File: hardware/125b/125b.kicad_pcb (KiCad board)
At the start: 2 copper layers, 54 x 60 mm, 56 parts, among them J1 Guitar in, J2 fsw pin 1, J3 fsw pin 2, J4 fsw pin 4, J5 fsw pin 5, J6 fsw pin 6, J7 Left out, J8 Right out, J9 fsw pin 3, SW1 Switch 1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

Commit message: Update PCB and resize for 125b
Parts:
- added J10: Barrel_Jack, Connector_BarrelJack:BarrelJack_Horizontal, F.Cu at (58.1, 52.3)
- added J11: NRJ6HF, Connector_Audio:Jack_6.35mm_Neutrik_NRJ6HF_Horizontal, F.Cu at (51.9, 32.2)
- added J7: fsw pin 3, Connector_Wire:SolderWire-0.25sqmm_1x01_D0.65mm_OD2mm, F.Cu at (75.5, 49.0)
- added J8: fsw pin 4, Connector_Wire:SolderWire-0.25sqmm_1x01_D0.65mm_OD2mm, F.Cu at (75.5, 53.0)
- added SW4: SW_DIP_x02, Button_Switch_SMD:SW_DIP_SPSTx02_Slide_9.78x7.26mm_W8.61mm_P2.54mm, F.Cu at (66.9, 51.4)
- J2: value fsw pin 1 -> fsw pin 7
- J4: value fsw pin 4 -> fsw pin 7
- J9: value fsw pin 3 -> fsw pin 1
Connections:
- C2 pad 1: Net-(J4-Pin_1) -> Net-(C2-Pad1)
- D2 pad 2: Net-(BT1-+) -> Net-(D2-A)
- R1 pad 1: Net-(BT1-+) -> Net-(D2-A)
- R2 pad 1: Net-(J4-Pin_1) -> Net-(C2-Pad1)
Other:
- board size 54 x 60 mm -> 59 x 75 mm

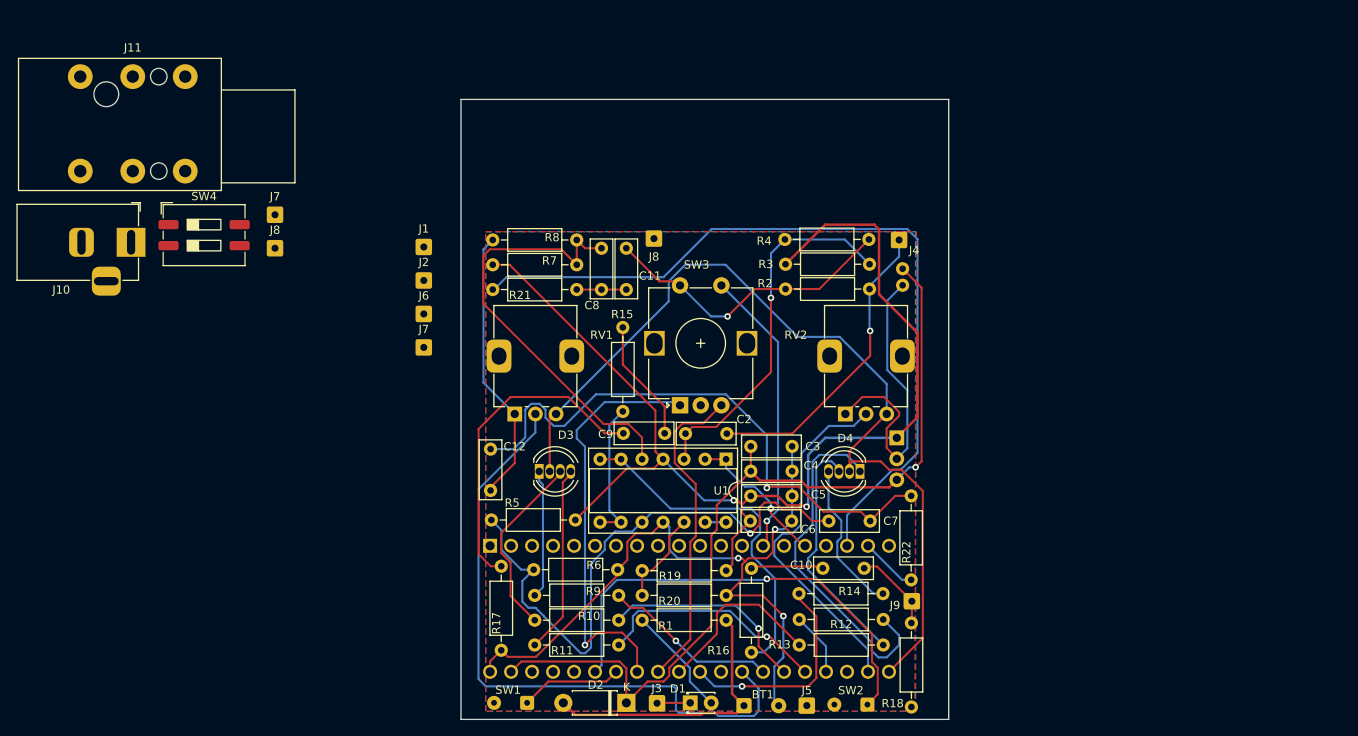
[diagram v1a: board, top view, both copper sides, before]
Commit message: Footprints for audio and power sockets added
Also DIP switch for line/ guitar input. Ready to start
moving components around.
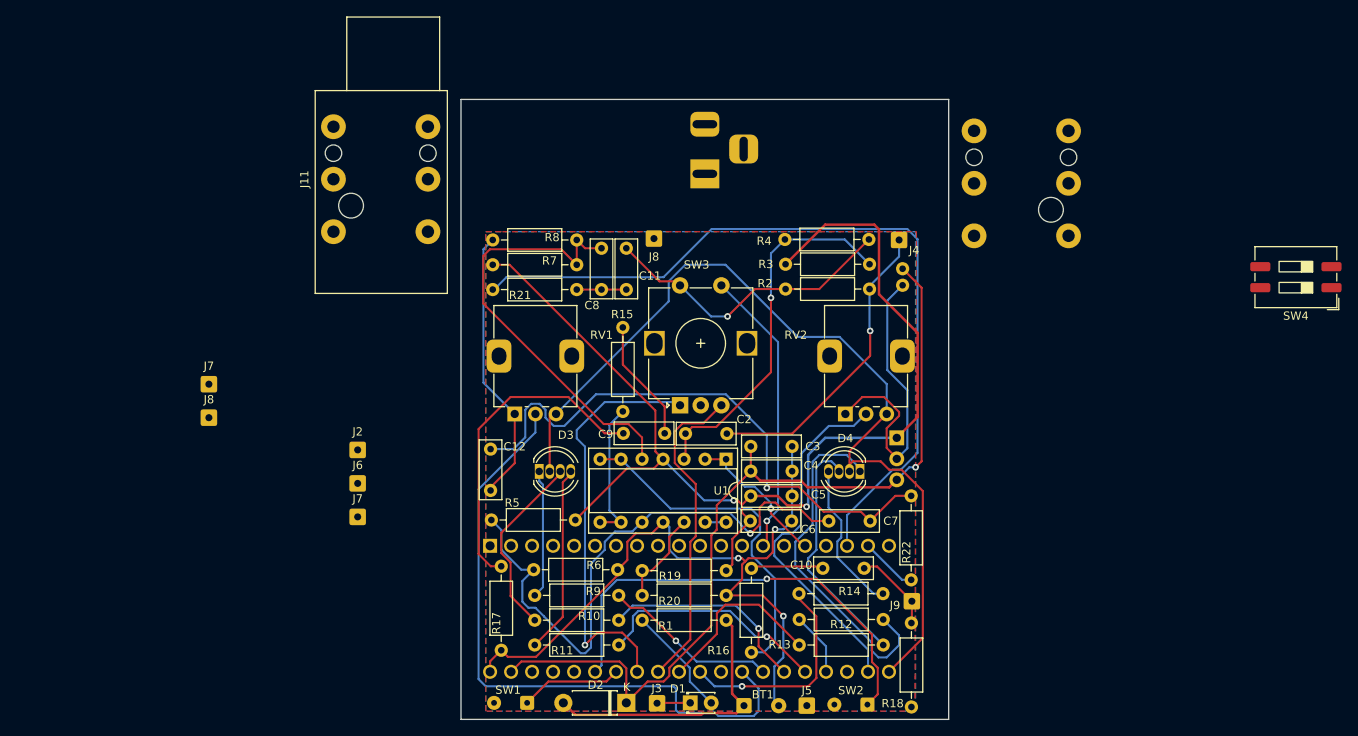
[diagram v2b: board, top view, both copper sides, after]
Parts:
- J1: footprint Connector_Wire:SolderWire-0.25sqmm_1x01_D0.65mm_OD2mm -> Connector_Audio:Jack_6.35mm_Neutrik_NRJ6HF-1-AU_Horizontal; moved to B.Cu
- J10: moved to B.Cu
- moved SW4 132.2 mm to (199.0, 56.5), turned to 180 degrees
- moved J1 78.0 mm to (171.5, 51.5), turned to 90 degrees
- moved J10 69.9 mm to (127.5, 44.0), turned to -90 degrees
- moved J11 35.9 mm to (82.6, 51.0), turned to 90 degrees
- moved J2 22.0 mm to (85.5, 77.4)
- moved J6 22.0 mm to (85.5, 81.5)
- moved J7 22.0 mm to (67.5, 69.5)
- moved J7 22.0 mm to (85.5, 85.5)
- moved J8 22.0 mm to (67.5, 73.5)

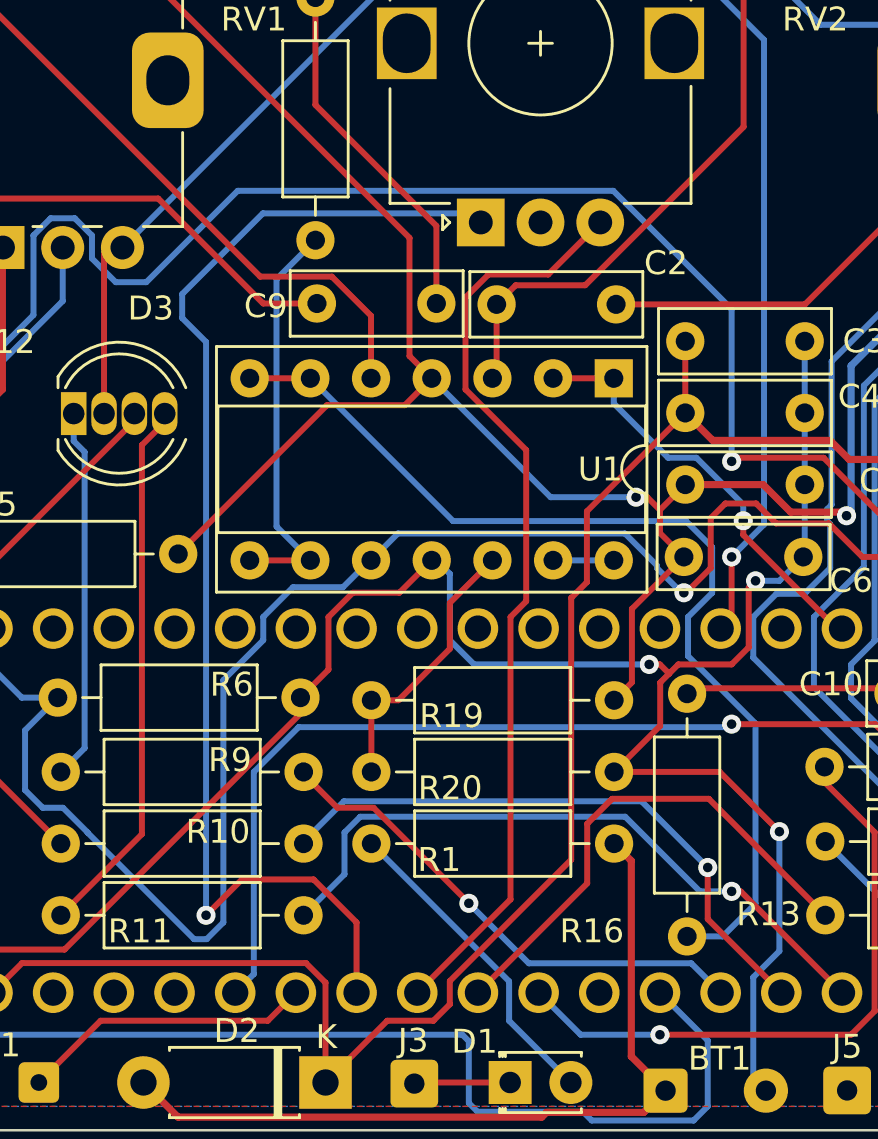
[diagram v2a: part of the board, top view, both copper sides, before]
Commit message: Swap encoder pins
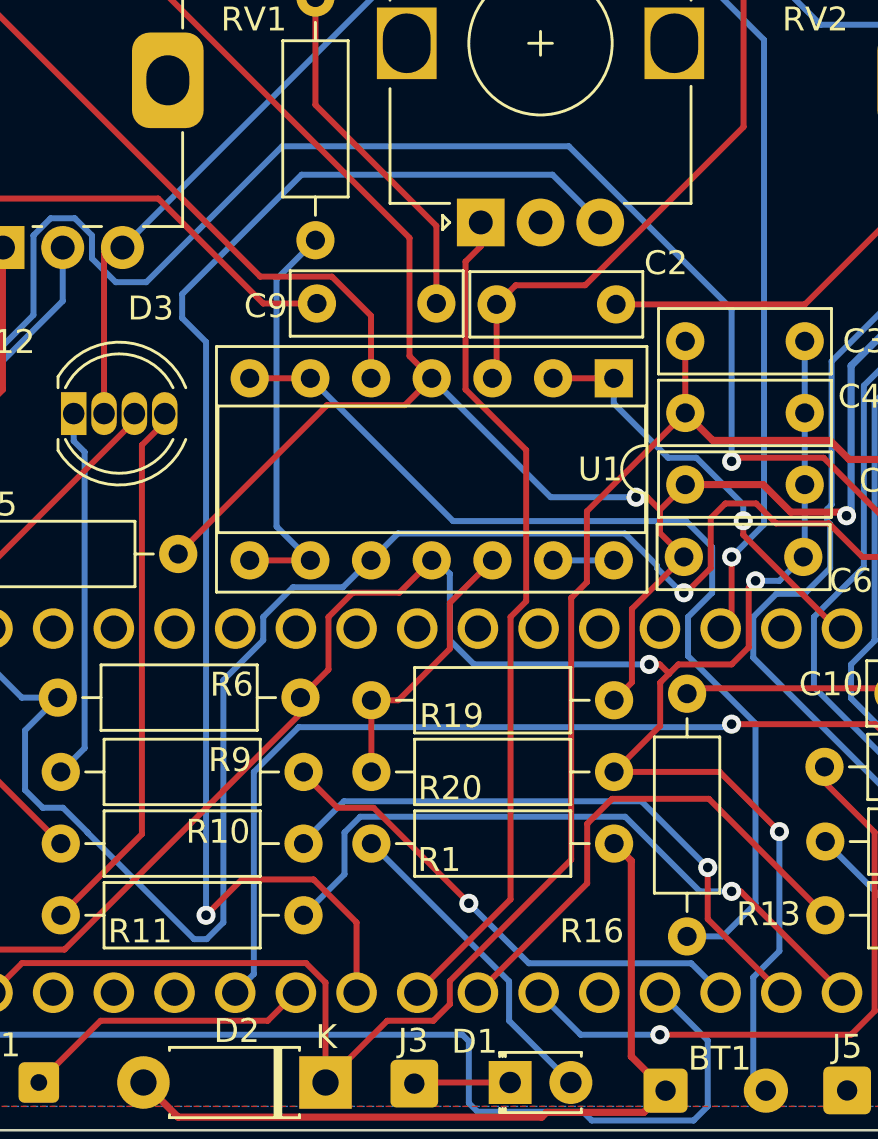
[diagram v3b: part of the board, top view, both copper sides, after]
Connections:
- A1 pad 32: Net-(A1-SAI2_SD_B) -> /ENC_A
- A1 pad 33: Net-(A1-SAI2_SD_A) -> /ENC_B
- SW3 pad A: Net-(A1-SAI2_SD_A) -> /ENC_A
- SW3 pad B: Net-(A1-SAI2_SD_B) -> /ENC_B
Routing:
- net /ENC_B: track 0.00 -> 57.4 mm, vias 0 -> 1
- net Net-(A1-SAI2_SD_A): track 52.0 -> 0.00 mm, vias 1 -> 0
- net Net-(A1-SAI2_SD_B): track 39.0 -> 0.00 mm
- net /ENC_A: track 0.00 -> 36.3 mm
- net Net-(C12-Pad2): track 69.8 -> 71.4 mm
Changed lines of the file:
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@@
 	(net 30 "/LED_2_B")
 	(net 31 "/LED_2_G")
-	(net 32 "Net-(A1-SAI2_SD_B)")
-	(net 33 "Net-(A1-SAI2_SD_A)")
+	(net 32 "/ENC_B")
+	(net 33 "/ENC_A")
 	(net 34 "Net-(A1-SAI2_FS)")
 	(net 35 "Net-(A1-SAI2_SCK)")
@@
 			(layers "*.Cu" "*.Mask")
 			(remove_unused_layers no)
-			(net 33 "Net-(A1-SAI2_SD_A)")
+			(net 33 "/ENC_A")
 			(pinfunction "A")
 			(pintype "passive")
@@
 			(layers "*.Cu" "*.Mask")
 			(remove_unused_layers no)
-			(net 32 "Net-(A1-SAI2_SD_B)")
+			(net 32 "/ENC_B")
 			(pinfunction "B")
 			(pintype "passive")
@@
 			(layers "*.Cu" "*.Mask")
 			(remove_unused_layers no)
-			(net 32 "Net-(A1-SAI2_SD_B)")
+			(net 33 "/ENC_A")
 			(pinfunction "SAI2_SD_B")
 			(pintype "bidirectional")
@@
 			(layers "*.Cu" "*.Mask")
 			(remove_unused_layers no)
-			(net 33 "Net-(A1-SAI2_SD_A)")
+			(net 32 "/ENC_B")
 			(pinfunction "SAI2_SD_A")
 			(pintype "bidirectional")
@@
 	)
 	(segment
-		(start 123.861294 78.98953)
-		(end 126.401294 81.52953)
+		(start 114.5 99.5)
+		(end 117.5 99.5)
 		(width 0.25)
 		(layer "F.Cu")
@@
 	)
 	(segment
-		(start 125.745 88.513299)
-		(end 125.745 100.335)
+		(start 113 101)
+		(end 114.5 99.5)
 		(width 0.25)
 		(layer "F.Cu")
@@
 	)
 	(segment
-		(start 123.861294 75.138992)
-		(end 123.861294 78.98953)
+		(start 119.3 101.3)
+		(end 119.3 104.24)
 		(width 0.25)
 		(layer "F.Cu")
@@
 	)
 	(segment
-		(start 126.401294 81.52953)
-		(end 126.401294 87.857005)
+		(start 117.5 99.5)
+		(end 119.3 101.3)
 		(width 0.25)
 		(layer "F.Cu")
 		(net 32)
 	)
-	(segment
-		(start 124.821859 74.178427)
-		(end 123.861294 75.138992)
-		(width 0.25)
-		(layer "F.Cu")
+	(via
+		(at 113 101)
+		(size 0.8)
+		(drill 0.4)
+		(layers "F.Cu" "B.Cu")
 		(net 32)
 	)
 	(segment
-		(start 127.321573 74.178427)
-		(end 124.821859 74.178427)
+		(start 112 75)
+		(end 117 70)
 		(width 0.25)
-		(layer "F.Cu")
+		(layer "B.Cu")
 		(net 32)
 	)
 	(segment
-		(start 125.745 100.335)
-		(end 121.84 104.24)
+		(start 112 76)
+		(end 112 75)
 		(width 0.25)
-		(layer "F.Cu")
+		(layer "B.Cu")
 		(net 32)
 	)
 	(segment
-		(start 129.5 72)
-		(end 127.321573 74.178427)
+		(start 117 70)
+		(end 127.5 70)
 		(width 0.25)
-		(layer "F.Cu")
+		(layer "B.Cu")
 		(net 32)
 	)
 	(segment
-		(start 126.401294 87.857005)
-		(end 125.745 88.513299)
+		(start 113 101)
+		(end 113 77)
 		(width 0.25)
-		(layer "F.Cu")
+		(layer "B.Cu")
 		(net 32)
 	)
 	(segment
-		(start 114.5 99.5)
-		(end 117.5 99.5)
+		(start 127.5 70)
+		(end 129.5 72)
 		(width 0.25)
-		(layer "F.Cu")
-		(net 33)
+		(layer "B.Cu")
+		(net 32)
 	)
 	(segment
-		(start 113 101)
-		(end 114.5 99.5)
+		(start 113 77)
+		(end 112 76)
 		(width 0.25)
-		(layer "F.Cu")
-		(net 33)
+		(layer "B.Cu")
+		(net 32)
 	)
 	(segment
-		(start 119.3 101.3)
-		(end 119.3 104.24)
+		(start 126.401294 81.52953)
+		(end 123.861294 78.98953)
 		(width 0.25)
 		(layer "F.Cu")
@@
 	)
 	(segment
-		(start 117.5 99.5)
-		(end 119.3 101.3)
+		(start 126.401294 87.857005)
+		(end 126.401294 81.52953)
 		(width 0.25)
 		(layer "F.Cu")
 		(net 33)
 	)
-	(via
-		(at 113 101)
-		(size 0.8)
-		(drill 0.4)
-		(layers "F.Cu" "B.Cu")
-		(net 33)
-	)
 	(segment
-		(start 112 75)
-		(end 112 76)
+		(start 124.5 73)
+		(end 124.5 72)
 		(width 0.25)
-		(layer "B.Cu")
+		(layer "F.Cu")
 		(net 33)
 	)
 	(segment
-		(start 115.381396 71.618604)
-		(end 112 75)
+		(start 123.861294 73.638706)
+		(end 124.5 73)
 		(width 0.25)
-		(layer "B.Cu")
+		(layer "F.Cu")
 		(net 33)
 	)
 	(segment
-		(start 124.118604 71.618604)
-		(end 115.381396 71.618604)
+		(start 123.861294 78.98953)
+		(end 123.861294 73.638706)
 		(width 0.25)
-		(layer "B.Cu")
+		(layer "F.Cu")
 		(net 33)
 	)
 	(segment
-		(start 124.5 72)
-		(end 124.118604 71.618604)
+		(start 125.745 100.335)
+		(end 125.745 88.513299)
 		(width 0.25)
-		(layer "B.Cu")
+		(layer "F.Cu")
 		(net 33)
 	)
 	(segment
-		(start 113 77)
-		(end 113 101)
+		(start 121.84 104.24)
+		(end 125.745 100.335)
 		(width 0.25)
-		(layer "B.Cu")
+		(layer "F.Cu")
 		(net 33)
 	)
 	(segment
-		(start 124.5 72)
-		(end 123.861294 72.638706)
+		(start 125.745 88.513299)
+		(end 126.401294 87.857005)
 		(width 0.25)
-		(layer "B.Cu")
+		(layer "F.Cu")
 		(net 33)
 	)
 	(segment
-		(start 112 76)
-		(end 113 77)
+		(start 123.861294 72.638706)
+		(end 124.5 72)
 		(width 0.25)
 		(layer "B.Cu")
@@
 	)
 	(segment
-		(start 101.576468 77.302941)
-		(end 104.349081 77.302941)
+		(start 107.507412 71.825)
+		(end 108.225 72.542588)
 		(width 0.25)
 		(layer "B.Cu")
@@
 	)
 	(segment
-		(start 135 75.626167)
-		(end 135 82)
+		(start 128.186966 68.813133)
+		(end 135 75.626167)
 		(width 0.25)
 		(layer "B.Cu")
@@
 	)
 	(segment
-		(start 109.217588 74.5)
-		(end 110.5 74.5)
+		(start 135 75.626167)
+		(end 135 82)
 		(width 0.25)
 		(layer "B.Cu")
@@
 	)
 	(segment
-		(start 110.5 74.5)
-		(end 114.325 70.675)
+		(start 101.576468 77.302941)
+		(end 104.349081 77.302941)
 		(width 0.25)
 		(layer "B.Cu")
@@
 	)
 	(segment
-		(start 108.225 72.542588)
-		(end 108.225 73.507412)
+		(start 104.349081 77.302941)
+		(end 105.775 75.877022)
 		(width 0.25)
 		(layer "B.Cu")
@@
 	)
 	(segment
-		(start 130.048833 70.675)
-		(end 135 75.626167)
+		(start 109.217588 74.5)
+		(end 110.5 74.5)
 		(width 0.25)
 		(layer "B.Cu")
@@
 	)
 	(segment
-		(start 105.775 72.542588)
-		(end 106.492588 71.825)
+		(start 116.186867 68.813133)
+		(end 128.186966 68.813133)
 		(width 0.25)
 		(layer "B.Cu")
@@
 	)
 	(segment
-		(start 104.349081 77.302941)
-		(end 105.775 75.877022)
+		(start 110.5 74.5)
+		(end 116.186867 68.813133)
 		(width 0.25)
 		(layer "B.Cu")
@@
 	)
 	(segment
-		(start 114.325 70.675)
-		(end 130.048833 70.675)
+		(start 105.775 72.542588)
+		(end 106.492588 71.825)
 		(width 0.25)
 		(layer "B.Cu")
@@
 	)
 	(segment
-		(start 108.225 73.507412)
-		(end 109.217588 74.5)
+		(start 108.225 72.542588)
+		(end 108.225 73.507412)
 		(width 0.25)
 		(layer "B.Cu")
@@
 	)
 	(segment
-		(start 107.507412 71.825)
-		(end 108.225 72.542588)
+		(start 108.225 73.507412)
+		(end 109.217588 74.5)
 		(width 0.25)
 		(layer "B.Cu")

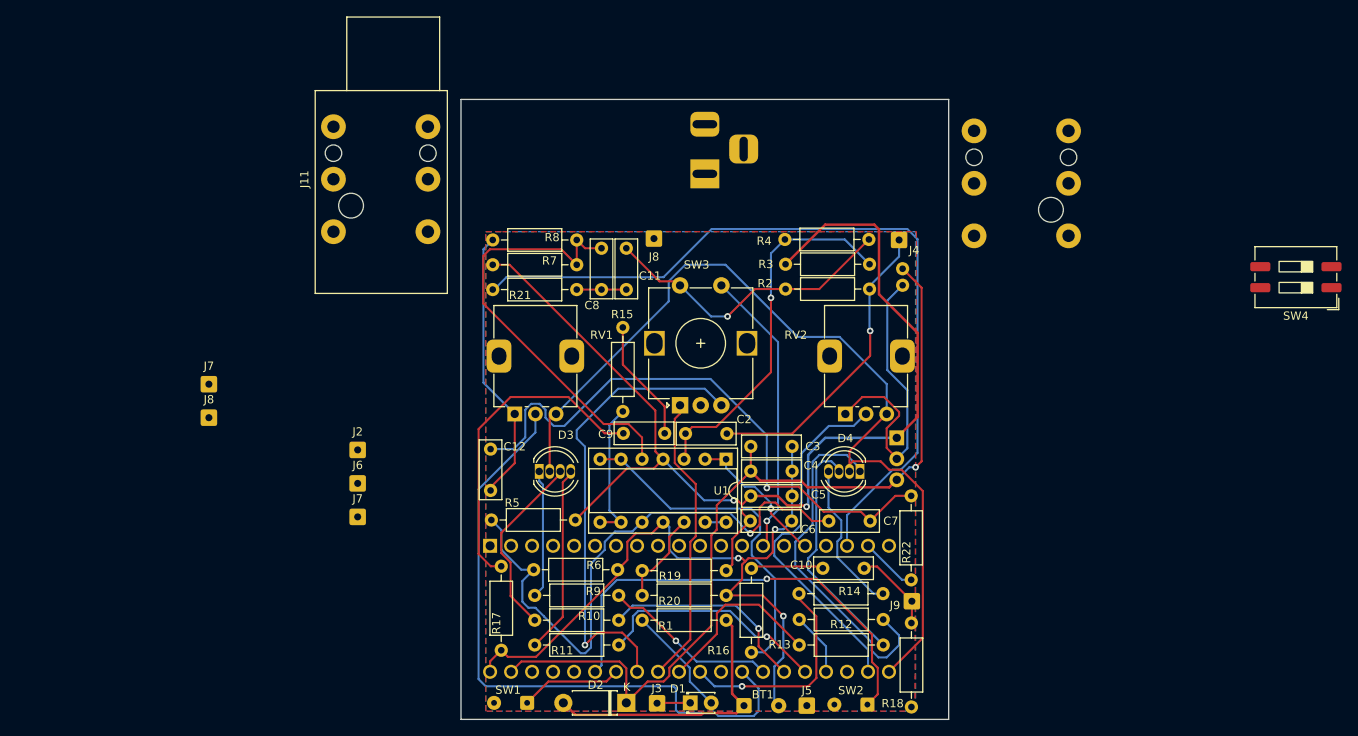
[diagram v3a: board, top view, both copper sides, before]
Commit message: Components replaced on board after rejig
Back with the audio and power sockets on board
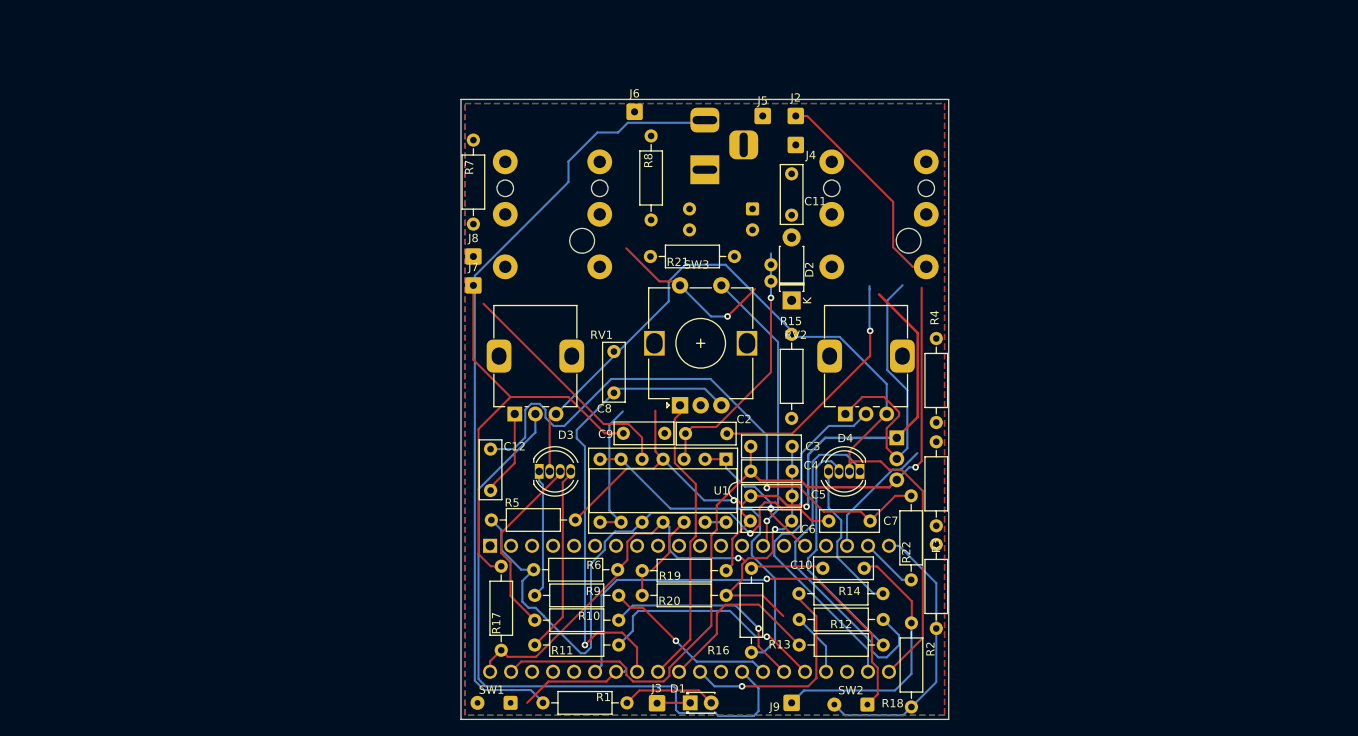
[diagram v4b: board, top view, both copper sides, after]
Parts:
- removed BT1: Battery_Cell, Connector_Wire:SolderWire-0.25sqmm_1x02_P4.2mm_D0.65mm_OD1.7mm
- removed the J7 at (85.5, 85.5)
- removed the J8 at (121.3, 51.8)
- J11: moved to B.Cu
- SW4: footprint Button_Switch_SMD:SW_DIP_SPSTx02_Slide_9.78x7.26mm_W8.61mm_P2.54mm -> Button_Switch_THT:SW_DIP_SPSTx02_Slide_9.78x7.26mm_W7.62mm_P2.54mm; moved to B.Cu
- moved J5 71.5 mm to (134.5, 37.0)
- moved J2 66.6 mm to (138.5, 37.0)
- moved SW4 66.2 mm to (133.3, 48.2)
- moved J6 56.1 mm to (119.0, 36.5)
- moved D2 52.6 mm to (138.0, 59.3), turned to 90 degrees
- moved J8 37.5 mm to (99.5, 54.0)
- moved R3 36.5 mm to (155.5, 86.6), turned to 90 degrees
- moved J7 34.2 mm to (99.5, 57.5)
- moved J11 32.5 mm to (114.8, 55.2)
- moved R2 31.9 mm to (155.5, 88.8), turned to -90 degrees
- moved R1 24.3 mm to (107.9, 108.0), turned to 0 degrees
- moved C11 21.9 mm to (138.0, 44.0)
- moved R4 21.9 mm to (155.5, 63.9), turned to -90 degrees
- moved R15 20.4 mm to (138.0, 73.6)
- moved R21 19.5 mm to (120.9, 54.0)
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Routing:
- net Net-(D2-A): track 0.00 -> 95.6 mm
- net /Left out: track 96.1 -> 15.3 mm
- net +5V: track 136.8 -> 88.4 mm
- net Net-(J4-Pin_1): track 36.8 -> 0.00 mm, vias 1 -> 0
- net Net-(BT1-+): track 34.1 -> 0.00 mm
- net Net-(C2-Pad1): track 0.00 -> 29.7 mm, vias 0 -> 1
- net Net-(J2-Pin_1): track 0.00 -> 26.6 mm
- net Net-(U1B-+): track 53.1 -> 28.5 mm
- net Net-(J9-Pin_1): track 10.8 -> 32.9 mm
- net GND: track 196.7 -> 179.9 mm, vias 4 -> 3
- net Net-(J7-Pin_1): track 39.4 -> 54.8 mm
- net Net-(C9-Pad1): track 14.9 -> 0.00 mm
- net Net-(U1A-+): track 44.8 -> 31.0 mm
- net /VCC: track 104.4 -> 97.0 mm
- net Net-(C11-Pad2): track 6.00 -> 0.00 mm
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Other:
- board text added: "Podal v0.4 Denis Crowdy"
- board text removed: "Podal v0.3 Denis Crowdy"
